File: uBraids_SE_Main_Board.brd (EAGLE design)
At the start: 40 x 115 mm, 106 parts, among them J1 JACK-THONKICONN, J2 JACK-THONKICONN, J3 JACK-THONKICONN, J4 JACK-THONKICONN, J5 JACK-THONKICONN, J6 JACK-THONKICONN, P1 10kB, P2 10kB, P3 10kB, P4 10kB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

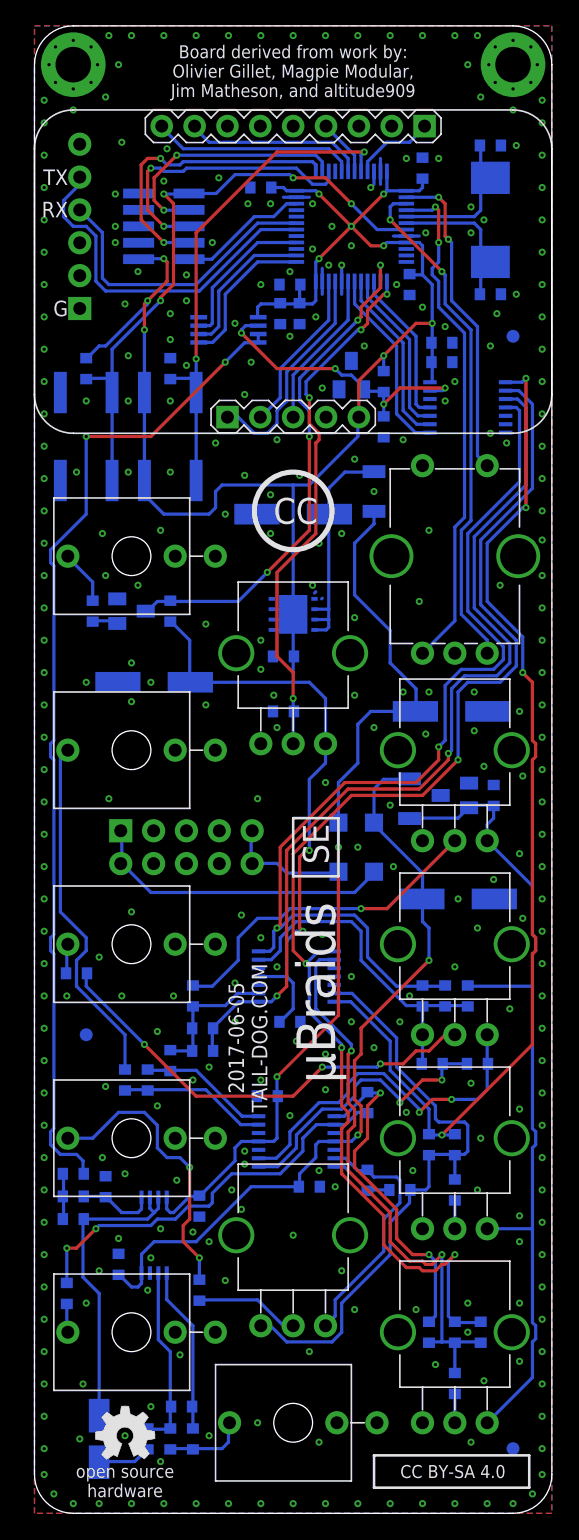
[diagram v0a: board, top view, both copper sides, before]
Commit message: revision C first pass, primarily to address rail clearance
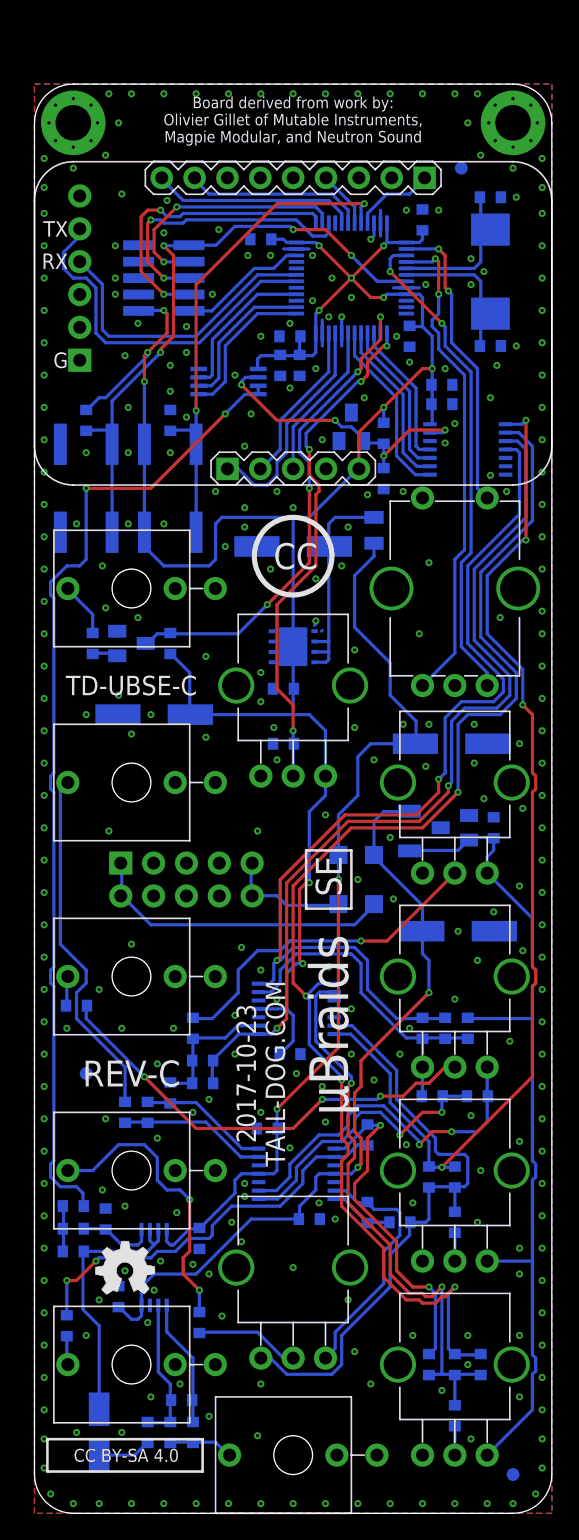
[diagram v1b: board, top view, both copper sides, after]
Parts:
- removed U$6: (no value), uBraids_SE:MARKING-UBRAIDS-SE
- R4: device uBraids_SE:1206-NP -> uBraids_SE:0805-NP
- moved U$1 25.3 mm to (7.00, 4.50)
- moved U$16 13.6 mm to (33.0, 104.0)
- moved U$8 12.8 mm to (7.00, 18.8)
- moved A1 4.00 mm to (0.00, 79.5)
- moved C1 4.00 mm to (35.2, 101.8)
- moved C11 4.00 mm to (27.0, 80.0)
- moved C2 4.00 mm to (30.0, 100.0)
- moved C3 4.00 mm to (17.5, 98.5)
- moved C4 4.00 mm to (29.0, 91.0)
- moved C5 4.00 mm to (19.8, 91.0)
- moved C6 4.00 mm to (35.2, 90.2)
- moved C7 4.00 mm to (20.5, 88.8)
- moved C8 4.00 mm to (19.0, 88.8)
- moved H1 4.00 mm to (10.0, 95.5)
- moved H2 4.00 mm to (3.50, 95.5)
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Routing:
- net N$75: track 14.2 -> 11.2 mm
- net N$73: track 12.9 -> 9.91 mm
- net N$67: track 24.1 -> 21.1 mm
- net GATE: track 39.7 -> 38.2 mm
- net FINE_TUNE: track 40.9 -> 39.4 mm
- net ENC_CLICK: track 24.8 -> 23.3 mm
- net ENC_B: track 39.5 -> 38.0 mm
- net ENC_A: track 39.6 -> 38.1 mm
- net N$72: track 6.21 -> 4.91 mm
- net AUDIO_OUT: track 77.5 -> 76.6 mm
- net PARAM2_CV: track 102.5 -> 101.8 mm
- net PARAM1_CV: track 82.4 -> 81.7 mm
- net FM_CV: track 75.8 -> 75.1 mm
- net ADC_SS: track 14.8 -> 14.0 mm
- net ADC_SCK: track 11.9 -> 11.2 mm
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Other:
- board size 40 x 115 mm -> 40 x 110.5 mm
- board text added: "2017-10-23"
- board text added: "2017-10-23 TALL-DOG.COM"
- board text added: "Board derived from work by: Olivier Gillet of Mutable Instruments, Magpie Modular, and Neutron Sound"
- board text added: "REV-C"
- board text added: "TD-UBSE-C"
- board text added: "µBraids_SE"
- board text removed: "2017-06-05"
- board text removed: "2017-06-05 TALL-DOG.COM"
- board text removed: "Board derived from work by: Olivier Gillet, Magpie Modular, Jim Matheson, and altitude909"
- board text removed: "open source hardware"

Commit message: removed additional 0.5 mm from main board, adjusted panel to match
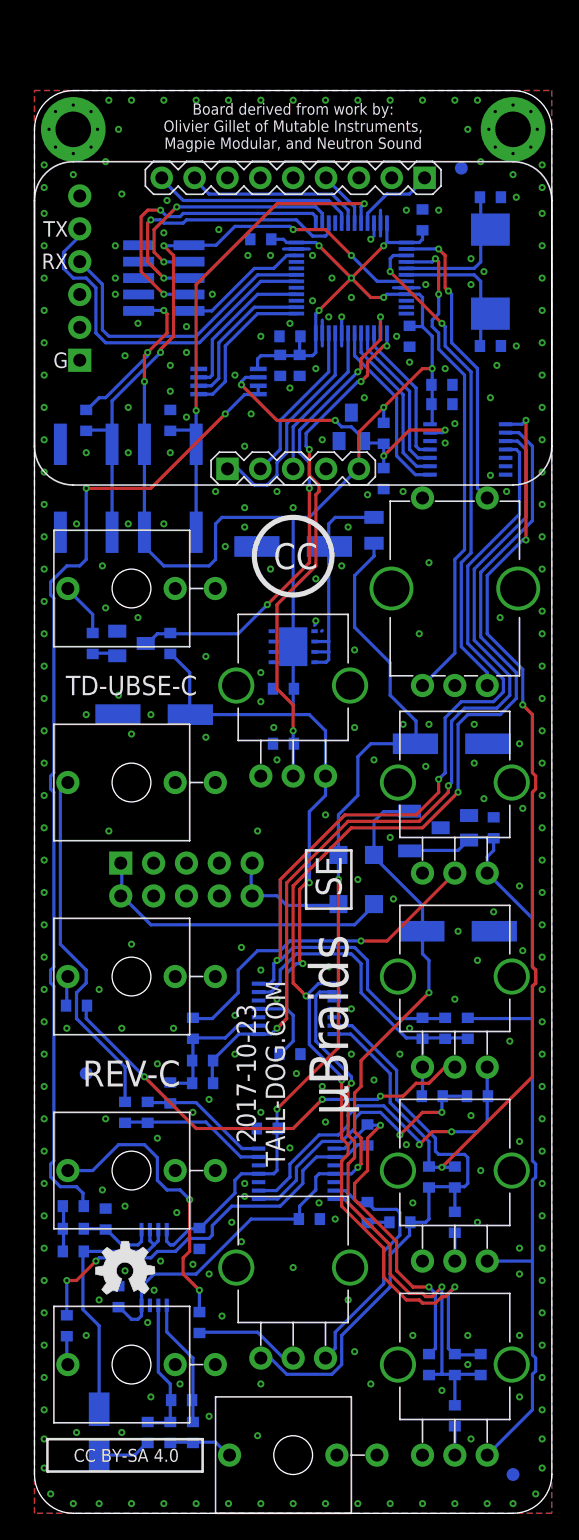
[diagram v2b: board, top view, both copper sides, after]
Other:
- board size 40 x 110.5 mm -> 40 x 110 mm
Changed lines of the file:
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@@
 <plain>
 <wire x1="3" y1="0" x2="37" y2="0" width="0" layer="20"/>
-<wire x1="40" y1="3" x2="40" y2="107.5" width="0" layer="20"/>
-<wire x1="37" y1="110.5" x2="3" y2="110.5" width="0" layer="20"/>
-<wire x1="0" y1="107.5" x2="0" y2="3" width="0" layer="20"/>
-<wire x1="0" y1="107.5" x2="3" y2="110.5" width="0" layer="20" curve="-90"/>
+<wire x1="40" y1="3" x2="40" y2="107" width="0" layer="20"/>
+<wire x1="37" y1="110" x2="3" y2="110" width="0" layer="20"/>
+<wire x1="0" y1="107" x2="0" y2="3" width="0" layer="20"/>
+<wire x1="0" y1="107" x2="3" y2="110" width="0" layer="20" curve="-90"/>
 <wire x1="3" y1="0" x2="0" y2="3" width="0" layer="20" curve="-90"/>
 <wire x1="40" y1="3" x2="37" y2="0" width="0" layer="20" curve="-90"/>
-<wire x1="37" y1="110.5" x2="40" y2="107.5" width="0" layer="20" curve="-90"/>
+<wire x1="37" y1="110" x2="40" y2="107" width="0" layer="20" curve="-90"/>
 <wire x1="4" y1="24.45" x2="4" y2="28" width="0.127" layer="22"/>
 <wire x1="4" y1="28" x2="4.75" y2="28" width="0.127" layer="22"/>
@@
 <wire x1="30.7" y1="38.5" x2="31.05" y2="38.5" width="0.127" layer="22"/>
 <wire x1="4" y1="23.05" x2="4" y2="22.7" width="0.127" layer="22"/>
-<circle x="3" y="107.5" radius="2.75" width="0" layer="41"/>
-<circle x="37" y="107.5" radius="2.75" width="0" layer="41"/>
-<circle x="3" y="107.5" radius="2.75" width="0" layer="42"/>
-<circle x="37" y="107.5" radius="2.75" width="0" layer="42"/>
-<text x="20" y="107.75" size="0.88" layer="22" ratio="10" rot="MR0" align="center">Board derived from work by:
+<circle x="3" y="107" radius="2.75" width="0" layer="41"/>
+<circle x="37" y="107" radius="2.75" width="0" layer="41"/>
+<circle x="3" y="107" radius="2.75" width="0" layer="42"/>
+<circle x="37" y="107" radius="2.75" width="0" layer="42"/>
+<text x="20" y="107.25" size="0.88" layer="22" ratio="10" rot="MR0" align="center">Board derived from work by:
 Olivier Gillet of Mutable Instruments,
 Magpie Modular, and Neutron Sound</text>
@@
 <vertex x="1.5" y="85"/>
 </polygon>
-<text x="20" y="107.75" size="0.88" layer="21" ratio="10" align="center">Board derived from work by:
+<text x="20" y="107.25" size="0.88" layer="21" ratio="10" align="center">Board derived from work by:
 Olivier Gillet of Mutable Instruments,
 Magpie Modular, and Neutron Sound</text>
@@
 <contactref element="C15" pad="C"/>
 <polygon width="0.125" layer="16" isolate="0.25">
-<vertex x="0" y="110.5"/>
-<vertex x="40" y="110.5"/>
+<vertex x="0" y="110"/>
+<vertex x="40" y="110"/>
 <vertex x="40" y="0"/>
 <vertex x="0" y="0"/>
 </polygon>
 <polygon width="0.125" layer="1" isolate="0.25">
-<vertex x="0" y="110.5"/>
-<vertex x="40" y="110.5"/>
+<vertex x="0" y="110"/>
+<vertex x="40" y="110"/>
 <vertex x="40" y="0"/>
 <vertex x="0" y="0"/>
@@
 <via x="39.25" y="100.5" extent="1-16" drill="0.25"/>
 <via x="39.25" y="102.5" extent="1-16" drill="0.25"/>
-<via x="20" y="109.75" extent="1-16" drill="0.25"/>
-<via x="17.5" y="109.75" extent="1-16" drill="0.25"/>
-<via x="15" y="109.75" extent="1-16" drill="0.25"/>
-<via x="12.5" y="109.75" extent="1-16" drill="0.25"/>
-<via x="10" y="109.75" extent="1-16" drill="0.25"/>
-<via x="7.5" y="109.75" extent="1-16" drill="0.25"/>
-<via x="22.5" y="109.75" extent="1-16" drill="0.25"/>
-<via x="25" y="109.75" extent="1-16" drill="0.25"/>
-<via x="27.5" y="109.75" extent="1-16" drill="0.25"/>
-<via x="30" y="109.75" extent="1-16" drill="0.25"/>
-<via x="32.5" y="109.75" extent="1-16" drill="0.25"/>
-<via x="5.75" y="109.75" extent="1-16" drill="0.25"/>
-<via x="0.75" y="104.75" extent="1-16" drill="0.25"/>
-<via x="34.25" y="109.75" extent="1-16" drill="0.25"/>
-<via x="39.25" y="104.75" extent="1-16" drill="0.25"/>
+<via x="20" y="109.25" extent="1-16" drill="0.25"/>
+<via x="17.5" y="109.25" extent="1-16" drill="0.25"/>
+<via x="15" y="109.25" extent="1-16" drill="0.25"/>
+<via x="12.5" y="109.25" extent="1-16" drill="0.25"/>
+<via x="10" y="109.25" extent="1-16" drill="0.25"/>
+<via x="7.5" y="109.25" extent="1-16" drill="0.25"/>
+<via x="22.5" y="109.25" extent="1-16" drill="0.25"/>
+<via x="25" y="109.25" extent="1-16" drill="0.25"/>
+<via x="27.5" y="109.25" extent="1-16" drill="0.25"/>
+<via x="30" y="109.25" extent="1-16" drill="0.25"/>
+<via x="32.5" y="109.25" extent="1-16" drill="0.25"/>
+<via x="5.75" y="109.25" extent="1-16" drill="0.25"/>
+<via x="0.75" y="104.25" extent="1-16" drill="0.25"/>
+<via x="34.25" y="109.25" extent="1-16" drill="0.25"/>
+<via x="39.25" y="104.25" extent="1-16" drill="0.25"/>
 <via x="6.75" y="102" extent="1-16" drill="0.25"/>
 <via x="6.25" y="98" extent="1-16" drill="0.25"/>
@@
 <via x="10" y="99" extent="1-16" drill="0.25"/>
 <via x="21.5" y="93.75" extent="1-16" drill="0.25"/>
-<via x="3" y="104" extent="1-16" drill="0.25"/>
-<via x="6.5" y="107.5" extent="1-16" drill="0.25"/>
-<via x="5.5" y="105" extent="1-16" drill="0.25"/>
-<via x="33.5" y="107.5" extent="1-16" drill="0.25"/>
-<via x="37" y="104" extent="1-16" drill="0.25"/>
-<via x="34.5" y="105" extent="1-16" drill="0.25"/>
+<via x="3" y="103.5" extent="1-16" drill="0.25"/>
+<via x="6.5" y="107" extent="1-16" drill="0.25"/>
+<via x="5.5" y="104.5" extent="1-16" drill="0.25"/>
+<via x="33.5" y="107" extent="1-16" drill="0.25"/>
+<via x="37" y="103.5" extent="1-16" drill="0.25"/>
+<via x="34.5" y="104.5" extent="1-16" drill="0.25"/>
 <via x="11.25" y="10" extent="1-16" drill="0.25"/>
 <via x="3.25" y="6.25" extent="1-16" drill="0.25"/>
@@
 </signal>
 <signal name="N$1">
-<via x="3" y="107.5" extent="1-16" drill="2.75" diameter="5"/>
+<via x="3" y="107" extent="1-16" drill="2.75" diameter="5"/>
 </signal>
 <signal name="N$2">
-<via x="37" y="107.5" extent="1-16" drill="2.75" diameter="5"/>
+<via x="37" y="107" extent="1-16" drill="2.75" diameter="5"/>
 </signal>
 <signal name="N$3">
-<via x="3" y="109.375" extent="1-16" drill="0.25"/>
+<via x="3" y="108.875" extent="1-16" drill="0.25"/>
 </signal>
 <signal name="N$4">
-<via x="3" y="105.625" extent="1-16" drill="0.25"/>
+<via x="3" y="105.125" extent="1-16" drill="0.25"/>
 </signal>
 <signal name="N$5">
-<via x="4.875" y="107.5" extent="1-16" drill="0.25"/>
+<via x="4.875" y="107" extent="1-16" drill="0.25"/>
 </signal>
 <signal name="N$6">
-<via x="1.125" y="107.5" extent="1-16" drill="0.25"/>
+<via x="1.125" y="107" extent="1-16" drill="0.25"/>
 </signal>
 <signal name="N$7">
-<via x="1.625" y="108.875" extent="1-16" drill="0.25"/>
+<via x="1.625" y="108.375" extent="1-16" drill="0.25"/>
 </signal>
 <signal name="N$8">
-<via x="4.375" y="108.875" extent="1-16" drill="0.25"/>
+<via x="4.375" y="108.375" extent="1-16" drill="0.25"/>
 </signal>
 <signal name="N$9">
-<via x="4.375" y="106.125" extent="1-16" drill="0.25"/>
+<via x="4.375" y="105.625" extent="1-16" drill="0.25"/>
 </signal>
 <signal name="N$10">
-<via x="1.625" y="106.125" extent="1-16" drill="0.25"/>
+<via x="1.625" y="105.625" extent="1-16" drill="0.25"/>
 </signal>
 <signal name="N$15">
-<via x="37" y="109.375" extent="1-16" drill="0.25"/>
+<via x="37" y="108.875" extent="1-16" drill="0.25"/>
 </signal>
 <signal name="N$16">
-<via x="37" y="105.625" extent="1-16" drill="0.25"/>
+<via x="37" y="105.125" extent="1-16" drill="0.25"/>
 </signal>
 <signal name="N$17">
-<via x="38.875" y="107.5" extent="1-16" drill="0.25"/>
+<via x="38.875" y="107" extent="1-16" drill="0.25"/>
 </signal>
 <signal name="N$18">
-<via x="35.125" y="107.5" extent="1-16" drill="0.25"/>
+<via x="35.125" y="107" extent="1-16" drill="0.25"/>
 </signal>
 <signal name="N$19">
-<via x="35.625" y="108.875" extent="1-16" drill="0.25"/>
+<via x="35.625" y="108.375" extent="1-16" drill="0.25"/>
 </signal>
 <signal name="N$20">
-<via x="38.375" y="108.875" extent="1-16" drill="0.25"/>
+<via x="38.375" y="108.375" extent="1-16" drill="0.25"/>
 </signal>
 <signal name="N$21">
-<via x="38.375" y="106.125" extent="1-16" drill="0.25"/>
+<via x="38.375" y="105.625" extent="1-16" drill="0.25"/>
 </signal>
 <signal name="N$22">
-<via x="35.625" y="106.125" extent="1-16" drill="0.25"/>
+<via x="35.625" y="105.625" extent="1-16" drill="0.25"/>
 </signal>
 </signals>

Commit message: prep for production of revision C
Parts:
- removed U$1: (no value), uBraids_SE:MARKING-CC-BY-SA-4.0
- removed U$3: (no value), uBraids_SE:MARKING-UBRAIDS-SE
- removed U$7: (no value), uBraids_SE:MARKING-CC-LOGO
- removed U$8: (no value), uBraids_SE:MARKING-OSH-LOGO-5MM
- added HOLE1, HOLE2: HOLE, uBraids_SE:M2.5-HOLE
- R7: device uBraids_SE:1206-NP -> uBraids_SE:0805-NP
- moved U$15 1.00 mm to (4.00, 35.0)
- moved A1 0.50 mm to (0.00, 80.0)
- moved C1 0.50 mm to (35.2, 102.2)
- moved C10 0.50 mm to (31.5, 86.2)
- moved C11 0.50 mm to (27.0, 80.5)
- moved C12 0.50 mm to (20.0, 75.2)
- moved C13 0.50 mm to (9.25, 62.2)
- moved C14 0.50 mm to (19.2, 64.2)
- moved C15 0.50 mm to (32.2, 60.0)
- moved C16 0.50 mm to (19.2, 60.0)
- moved C17 0.50 mm to (35.5, 53.5)
- moved C18 0.50 mm to (32.8, 45.5)
- moved C19 0.50 mm to (31.8, 38.0)
- moved C2 0.50 mm to (30.0, 100.5)
- moved C20 0.50 mm to (19.8, 36.0)
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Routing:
- net -12V: track 60.5 -> 60.0 mm
- net GND: vias 300 -> 301
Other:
- board size 40 x 110 mm -> 40 x 110.5 mm
- board text added: "2017-10-24"
- board text added: "GN"
- board text added: "µBraids_SE TD-UBSE-C 2017-10-24 TALL-DOG.COM CC BY-SA 4.0"
- board text removed: "2017-10-23"
- board text removed: "2017-10-23 TALL-DOG.COM"
- board text removed: "G"
- board text removed: "REV-C"
